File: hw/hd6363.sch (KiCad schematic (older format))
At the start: 5 parts, among them U1 XTAL_OSC_HALF_CAN, U2 MAX708, U3 HD6303RP

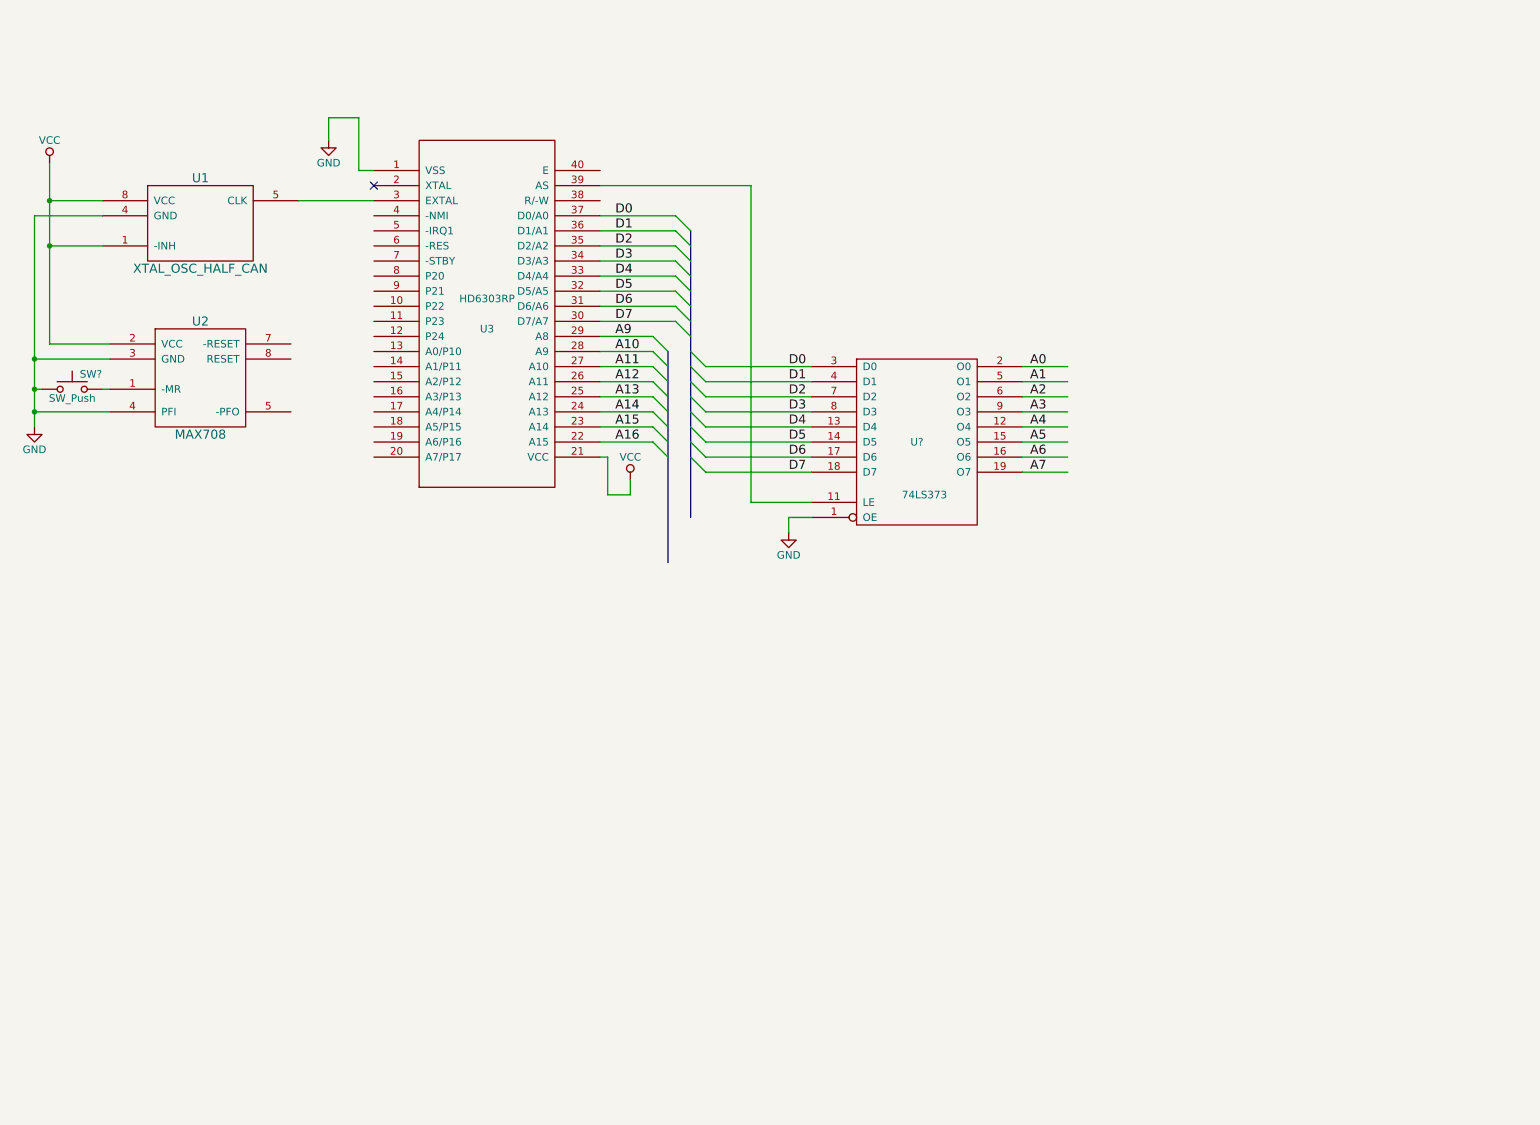
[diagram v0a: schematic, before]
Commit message: basic circuit is in place
If I do say so myself, I found a pretty clever way to
implement a nice memory map for ROM, RAM, and I/O,
using only '02, '32, and '138 chips, with no unused
gates.
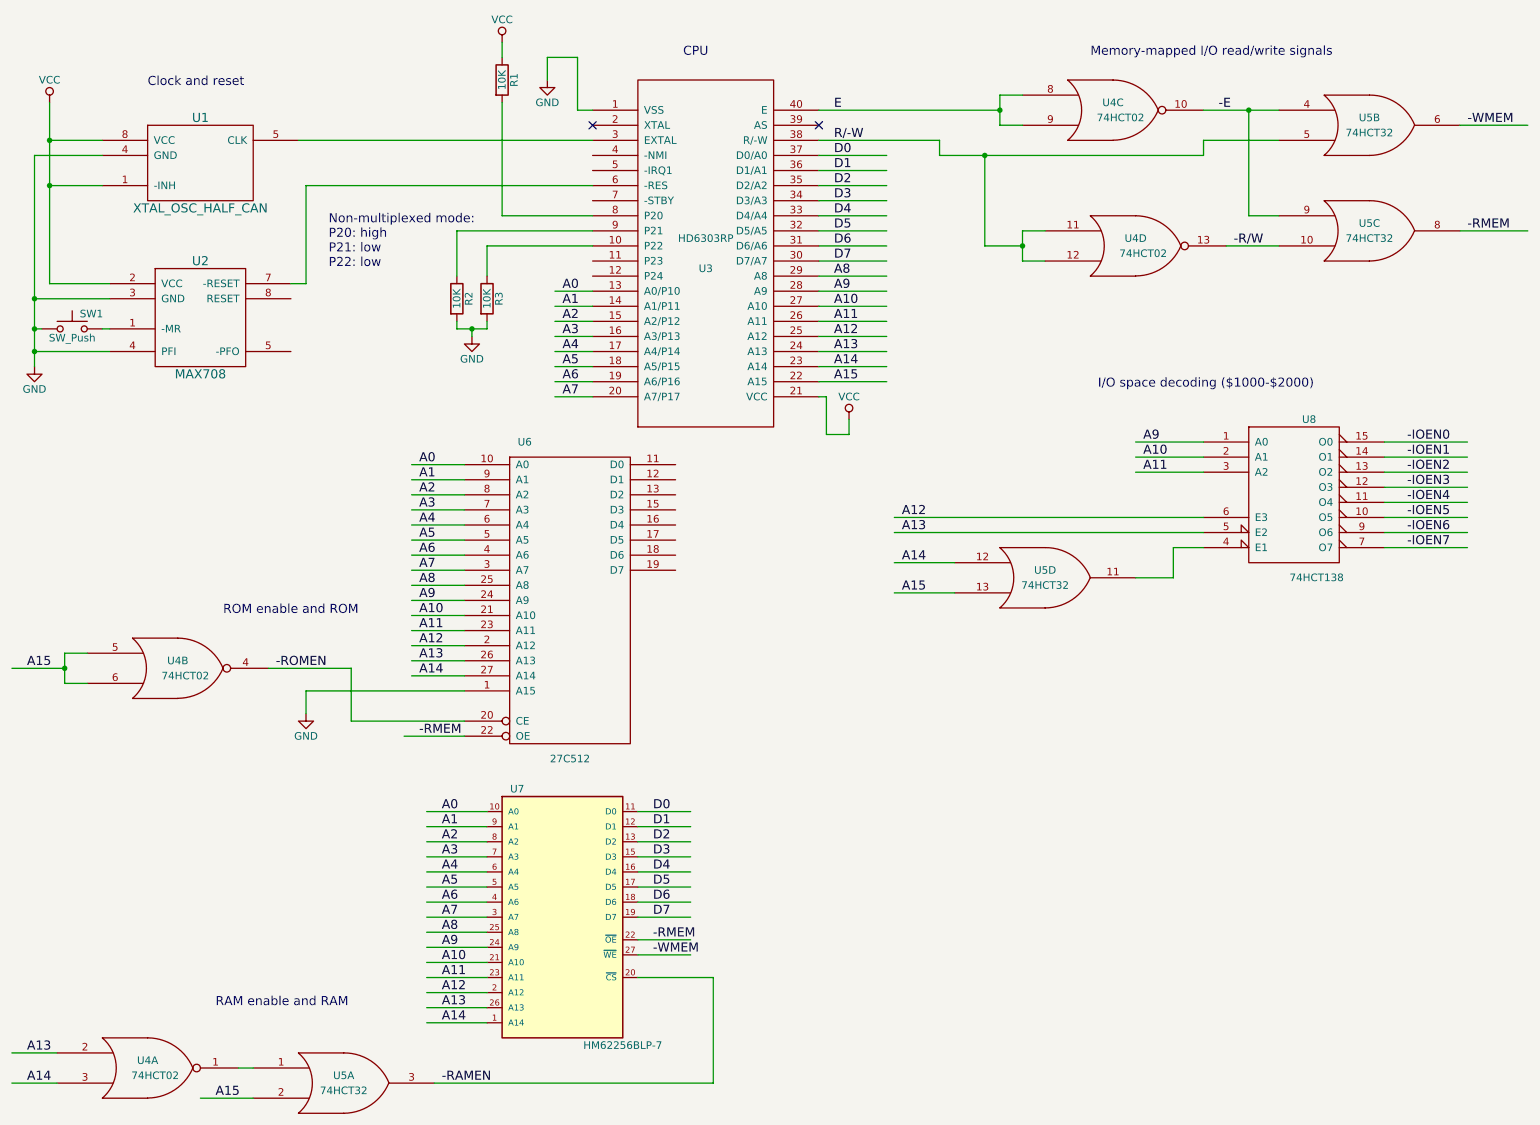
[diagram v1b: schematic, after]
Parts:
- removed U?: 74LS373, symbol 74LS373
- added R1, R2, R3: 10K, symbol R
- added U4: 74HCT02, symbol 74LS02
- added U5: 74HCT32, symbol 74LS32
- added U6: 27C512, symbol 27C512
- added U7: HM62256BLP-7, DIP28, symbol HM62256BLP-7
- added U8: 74HCT138, symbol 74LS138
- gave numbers to parts that had none: 1
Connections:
- net labels added: -E, -IOEN0, -IOEN1, -IOEN2, -IOEN3, -IOEN4, -IOEN5, -IOEN6, -IOEN7, -R/W, -RAMEN, -RMEM, -ROMEN, -WMEM, A8, E, R/-W
- net labels removed: A16
- wire segments 56 -> 152
- no-connect marks 1 -> 2
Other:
- note added: "CPU"
- note added: "Clock and reset"
- note added: "I/O space decoding ($1000-$2000)"
- note added: "Memory-mapped I/O read/write signals"
- note added: "Non-multiplexed mode:\nP20: high\nP21: low\nP22: low"
- note added: "RAM enable and RAM"
- note added: "ROM enable and ROM"
- moved on the sheet: SW1, U1, U2, U3

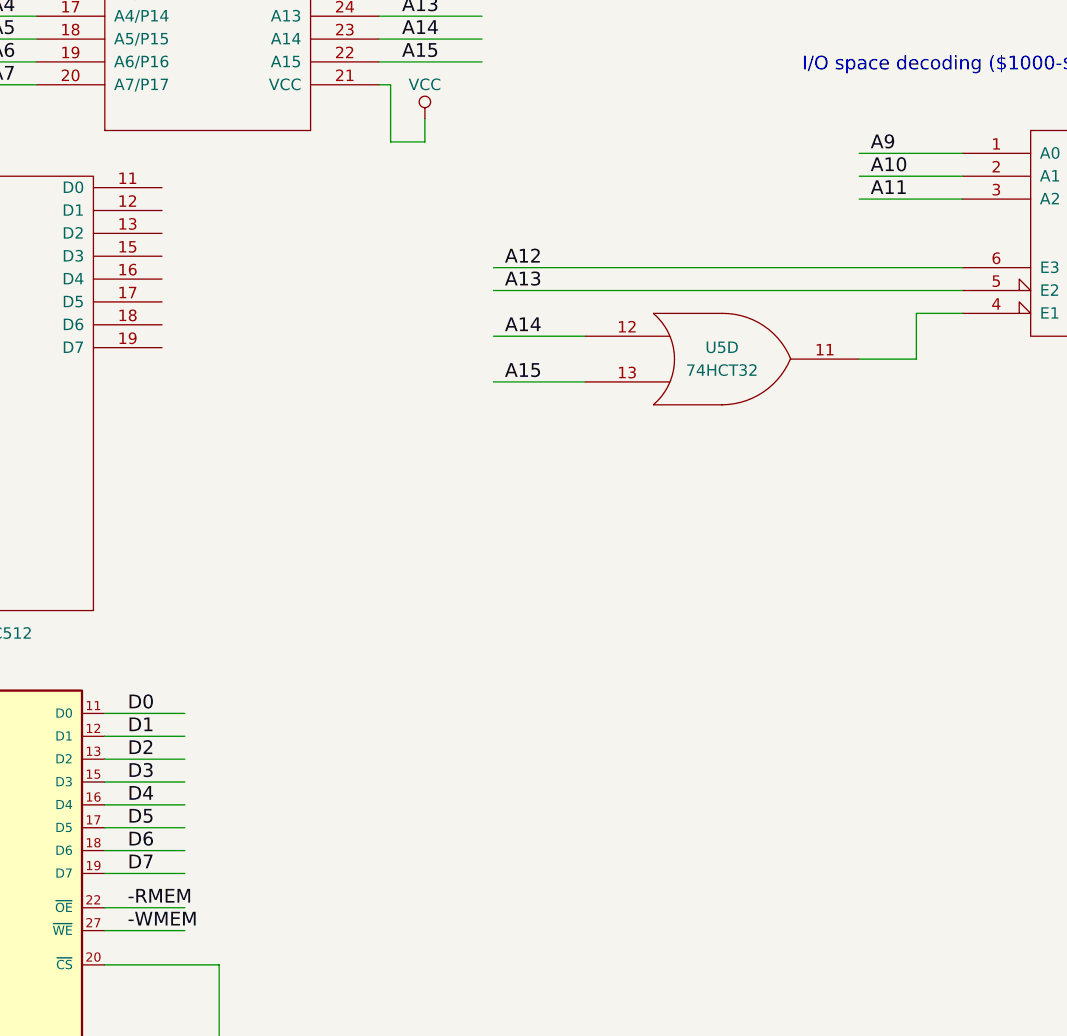
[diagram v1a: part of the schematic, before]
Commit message: added an output port
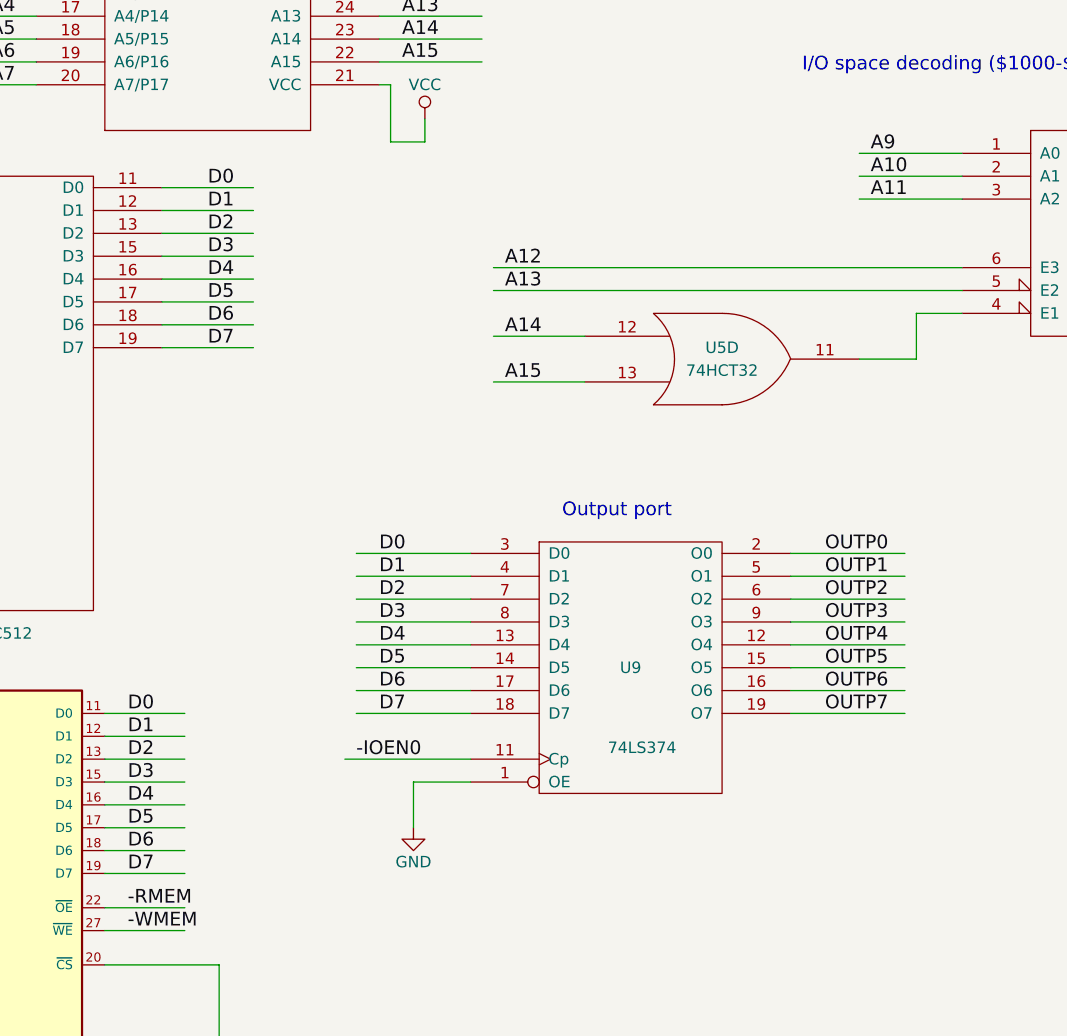
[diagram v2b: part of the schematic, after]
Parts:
- added U9: 74LS374, symbol 74LS374
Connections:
- net labels added: OUTP0, OUTP1, OUTP2, OUTP3, OUTP4, OUTP5, OUTP6, OUTP7
- wire segments 152 -> 179
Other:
- note added: "Output port"
